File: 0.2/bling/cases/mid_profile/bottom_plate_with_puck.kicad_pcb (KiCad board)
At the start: 2 copper layers, 110.3 x 98 mm, 0 parts

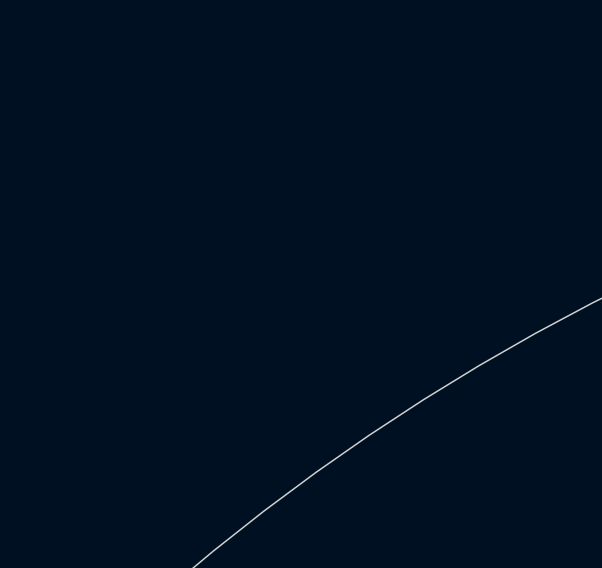
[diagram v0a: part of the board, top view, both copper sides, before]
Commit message: Add dummy component to each plate case
This works around a segfault in Pcbdraw which prevents renders in the
edge case where a PCB file has no module.
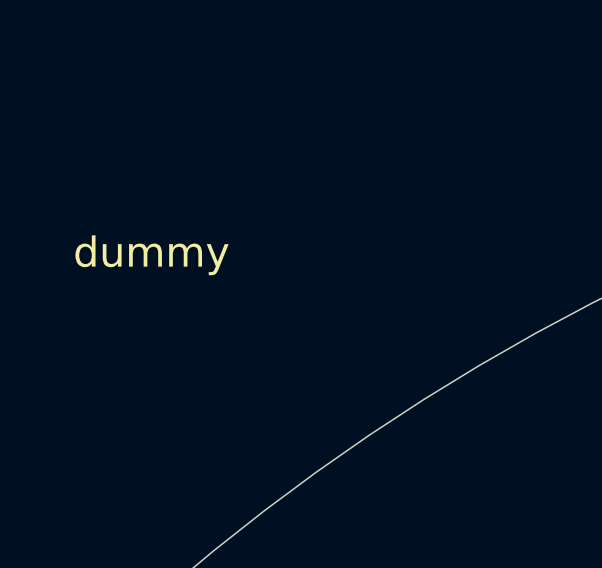
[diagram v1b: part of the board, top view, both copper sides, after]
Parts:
- added dummy: dummy, dummy:dummy, F.Cu at (12.0, 12.0)
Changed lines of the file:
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@@
     (tracks 0)
     (zones 0)
-    (modules 0)
+    (modules 1)
     (nets 1)
   )
@@
     (uvia_drill 0.1)
   )
+  (module dummy:dummy (layer F.Cu)
+    (at 12 12)
+    (fp_text reference dummy (at 0 0.5) (layer F.SilkS)
+      (effects (font (size 1 1) (thickness 0.15)))
+    )
+    (fp_text value dummy (at 0 -0.5) (layer F.Fab)
+      (effects (font (size 1 1) (thickness 0.15)))
+    )
+  )
   (gr_circle (center 67.790402 38.02) (end 46.780402 37.89) (layer Edge.Cuts) (width 0.05))
